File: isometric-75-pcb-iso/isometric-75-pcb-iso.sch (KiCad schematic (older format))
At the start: 26 parts, among them J101 Conn_01x06_Male, Q101 AO3400A, SW101 RST, SW102 BOOT, U101 XC6206P332MR, U102 STM32F072CBTx

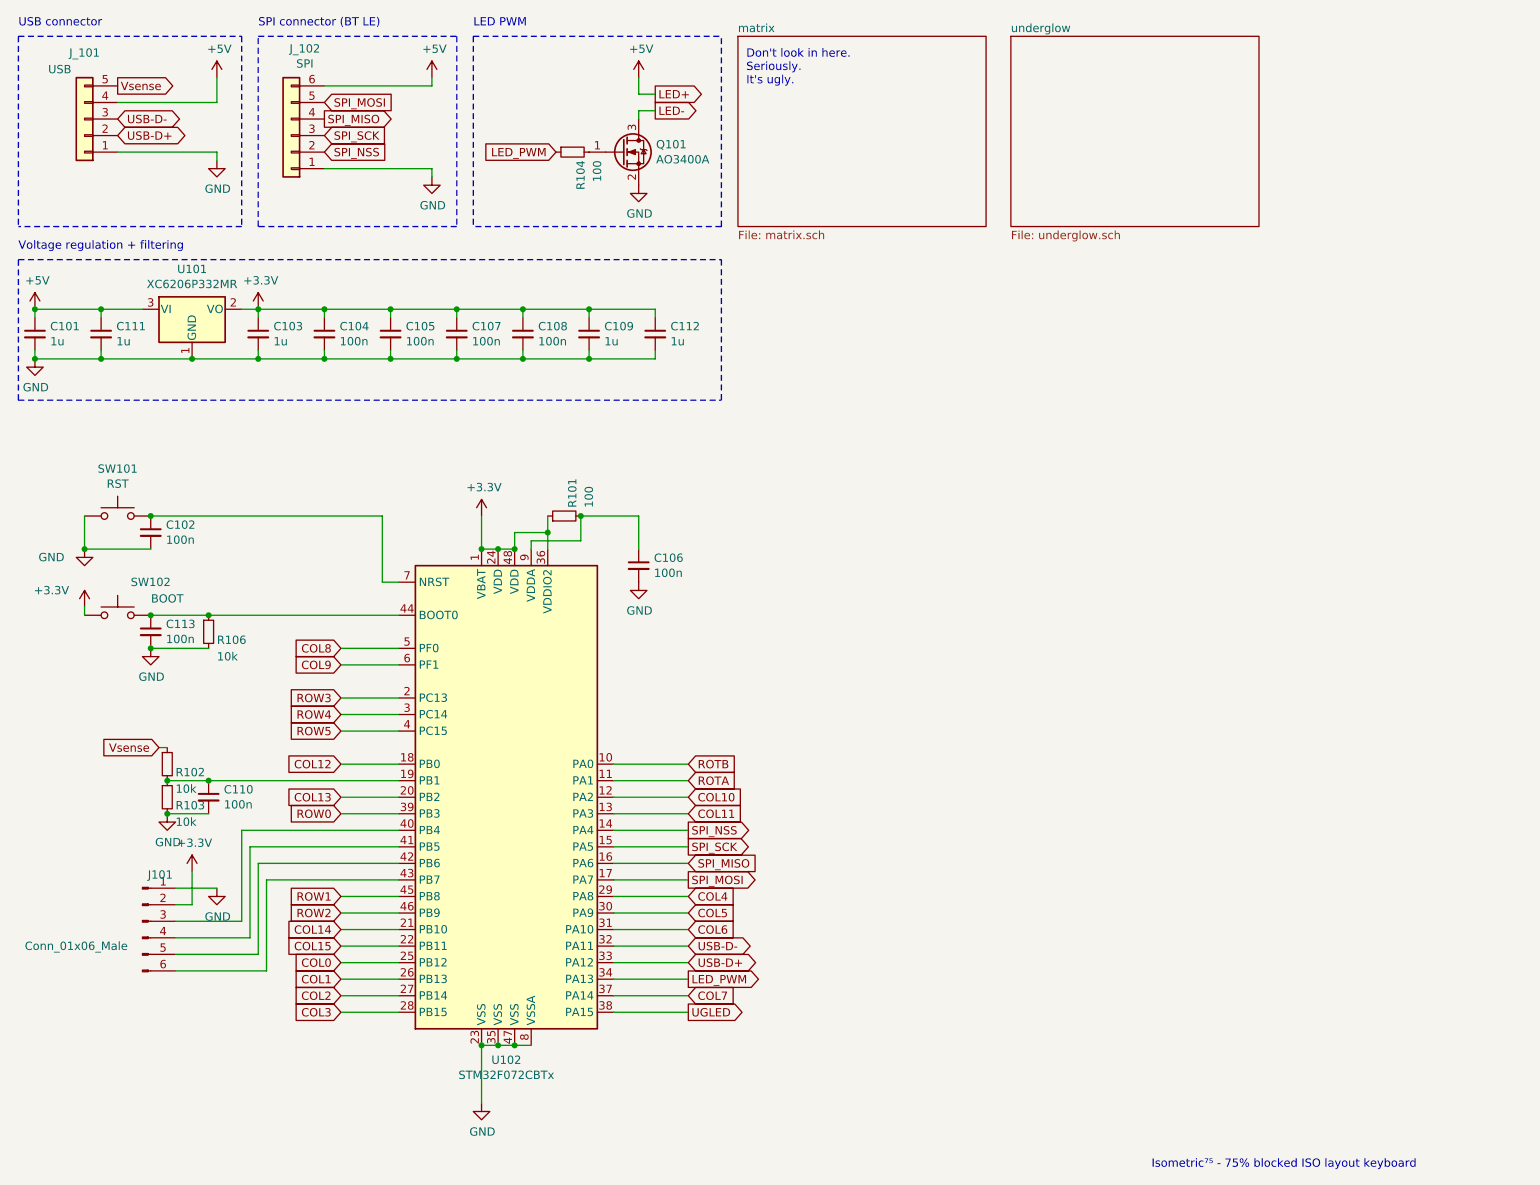
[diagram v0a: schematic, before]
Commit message: cosmethical changes, fixed a footprint collision
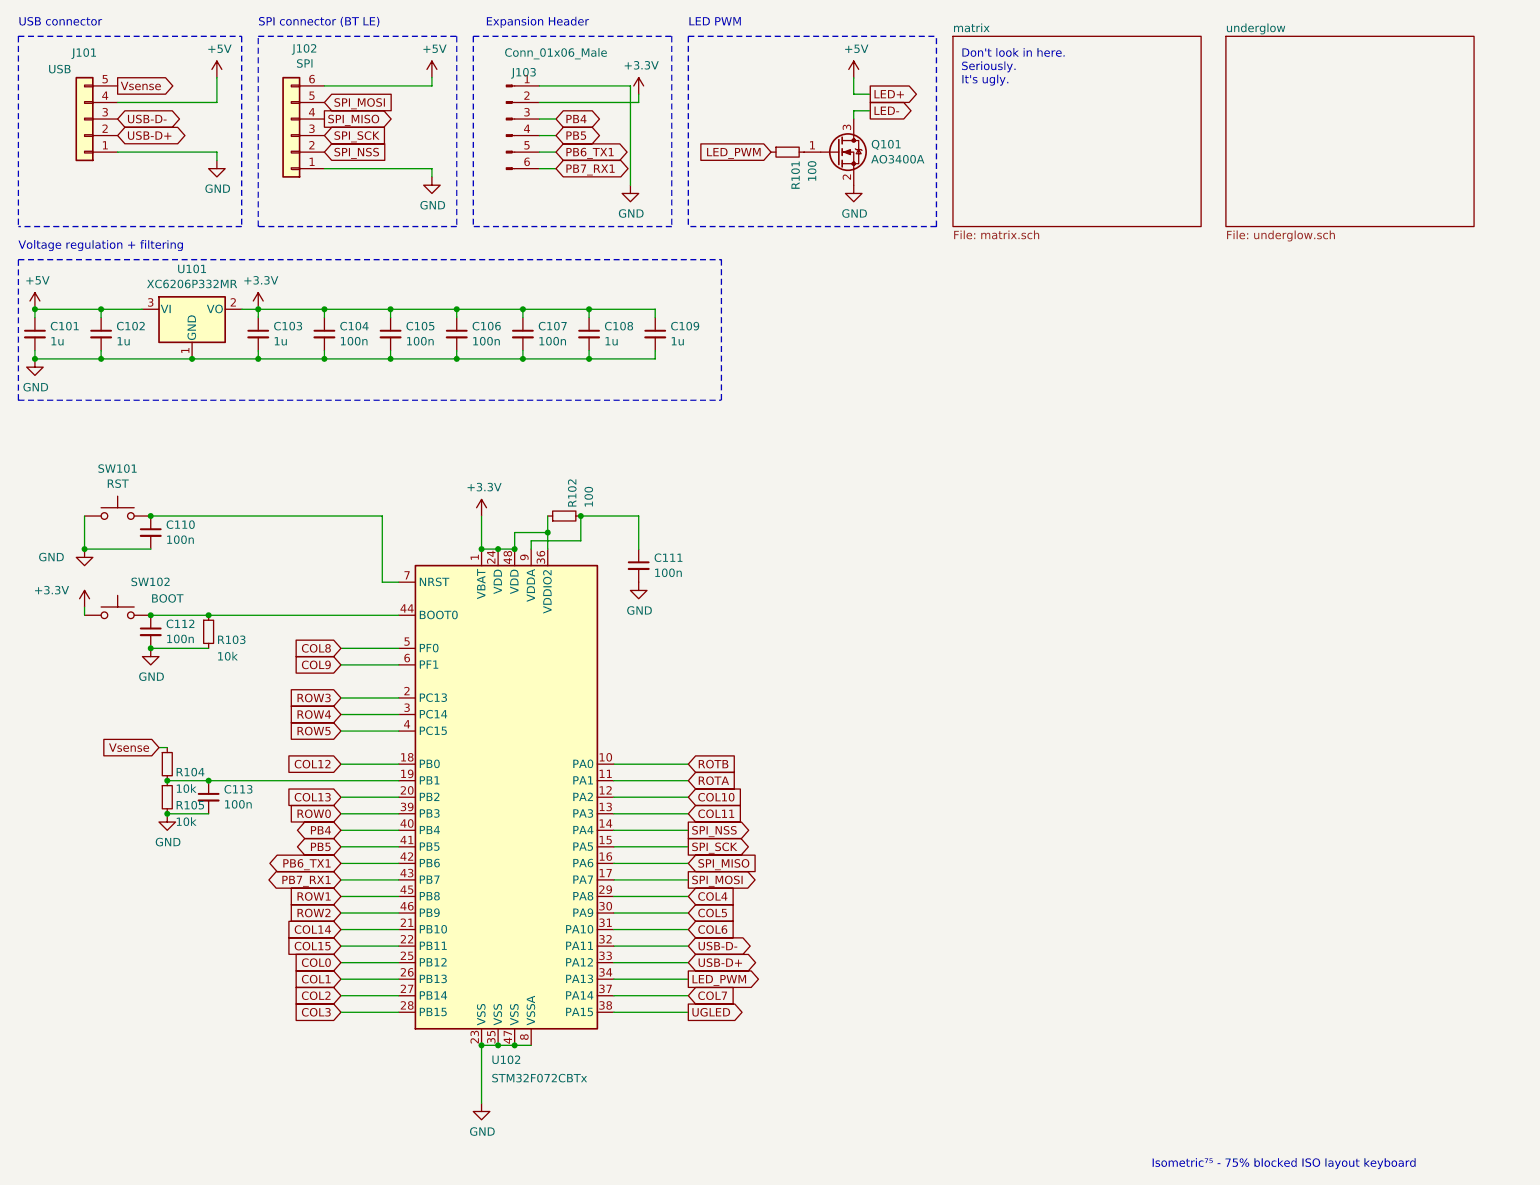
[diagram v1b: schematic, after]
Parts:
- renumbered C111 to C102, C107 to C106, C108 to C107, C109 to C108, C112 to C109, C102 to C110, C106 to C111, C113 to C112, C110 to C113, J_101 to J101, J_102 to J102, J101 to J103, R104 to R101, R101 to R102, R106 to R103, R102 to R104, R103 to R105
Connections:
- net PB4: now reaches J103.3 (Pin_3), U102.40 (PB4)
- net PB5: now reaches J103.4 (Pin_4), U102.41 (PB5)
- net PB6_TX1: now reaches J103.5 (Pin_5), U102.42 (PB6)
- net PB7_RX1: now reaches J103.6 (Pin_6), U102.43 (PB7)
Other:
- note added: "Expansion Header"
- moved on the sheet: J103, Q101, R101

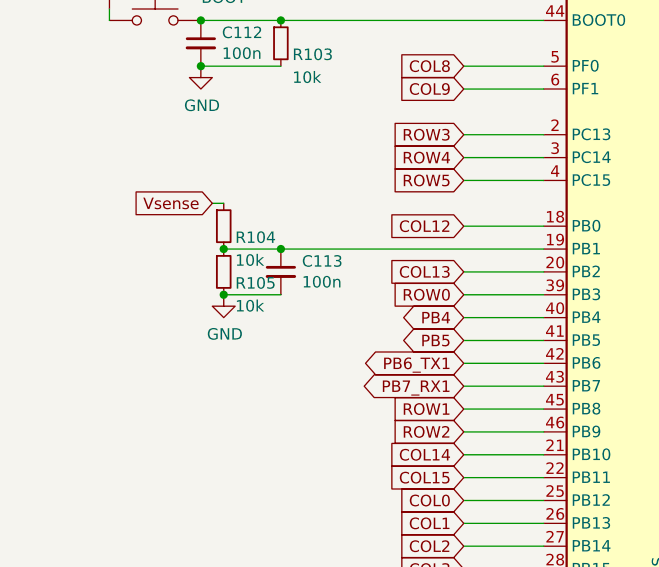
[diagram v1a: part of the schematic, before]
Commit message: changed divider resistors to save power
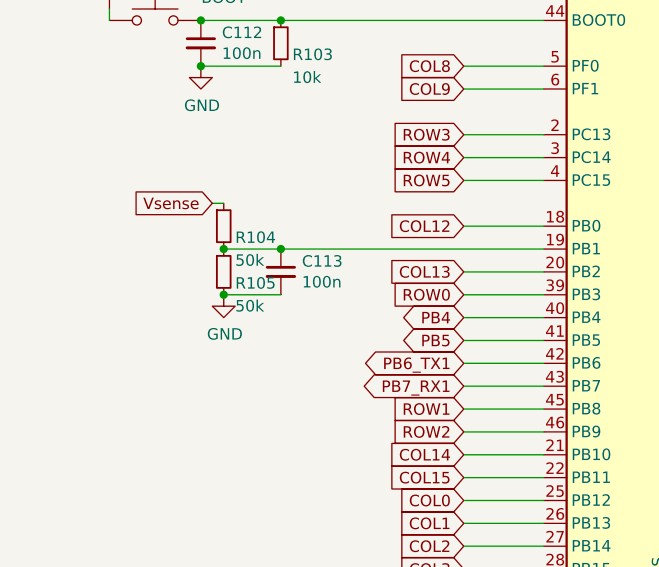
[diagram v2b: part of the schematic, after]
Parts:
- R104, R105: value 10k -> 50k
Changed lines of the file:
@@
 P 1450 5250
 F 0 "R105" H 1500 5200 50  0000 L CNN
-F 1 "10k" H 1500 5100 50  0000 L CNN
+F 1 "50k" H 1500 5100 50  0000 L CNN
 F 2 "Resistor_SMD:R_0402_1005Metric" H 1450 5250 50  0001 C CNN
 F 3 "~" H 1450 5250 50  0001 C CNN
@@
 P 1450 5050
 F 0 "R104" H 1500 5000 50  0000 L CNN
-F 1 "10k" H 1500 4900 50  0000 L CNN
+F 1 "50k" H 1500 4900 50  0000 L CNN
 F 2 "Resistor_SMD:R_0402_1005Metric" H 1450 5050 50  0001 C CNN
 F 3 "~" H 1450 5050 50  0001 C CNN

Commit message: minor layout fixes (thanks gLu3xb3rchi)
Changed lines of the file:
@@
 $EndComp
 Text GLabel 5700 1000 2    50   Output ~ 0
-LED+
++5V
 Text GLabel 5700 1100 2    50   Output ~ 0
 LED-
